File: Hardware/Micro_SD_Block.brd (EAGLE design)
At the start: 30.5 x 44.5 mm, 19 parts, among them U1 USD-SOCKETNEW, U2 EDISON_CONNECTOR_FULLMOUNTING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, U3 EDISON_CONNECTOR_FULLHEADER

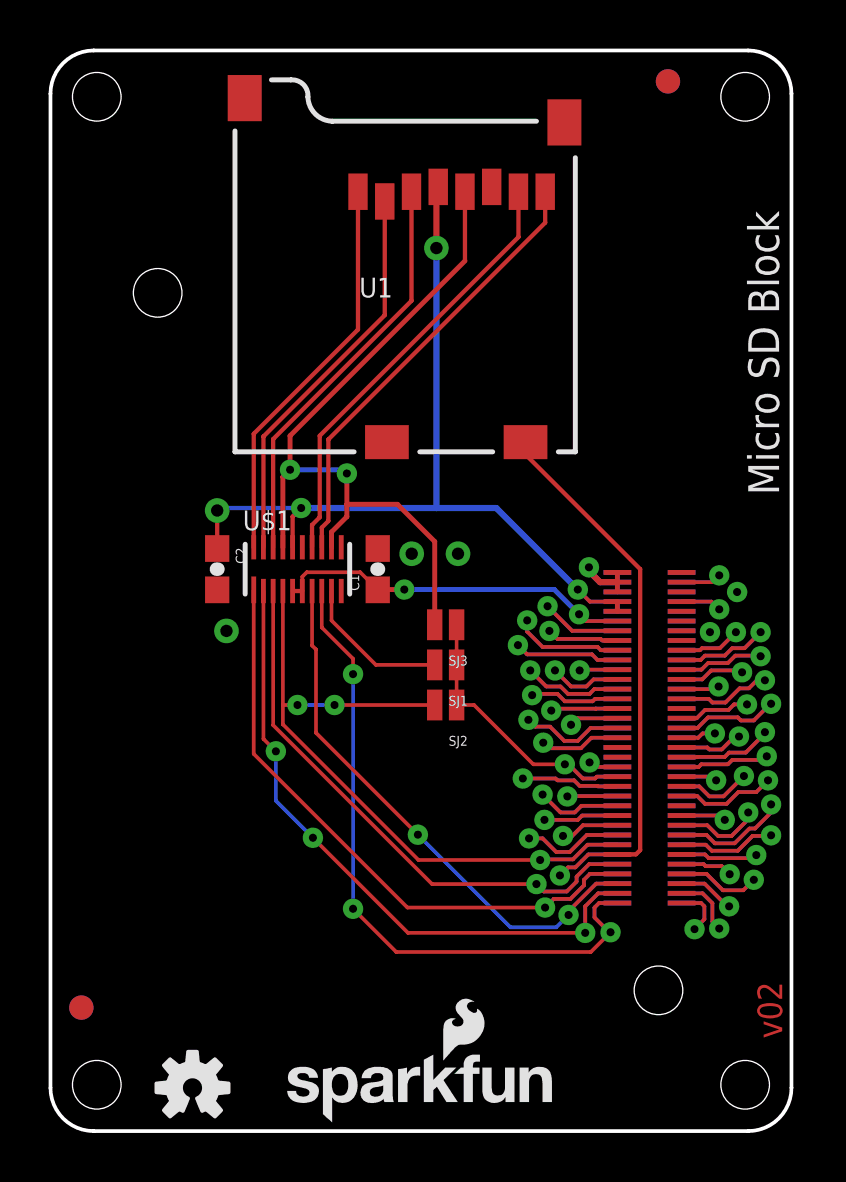
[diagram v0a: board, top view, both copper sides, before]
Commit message: removed thermals on connectors updated connector to new foot print updated version number corrected silk positions
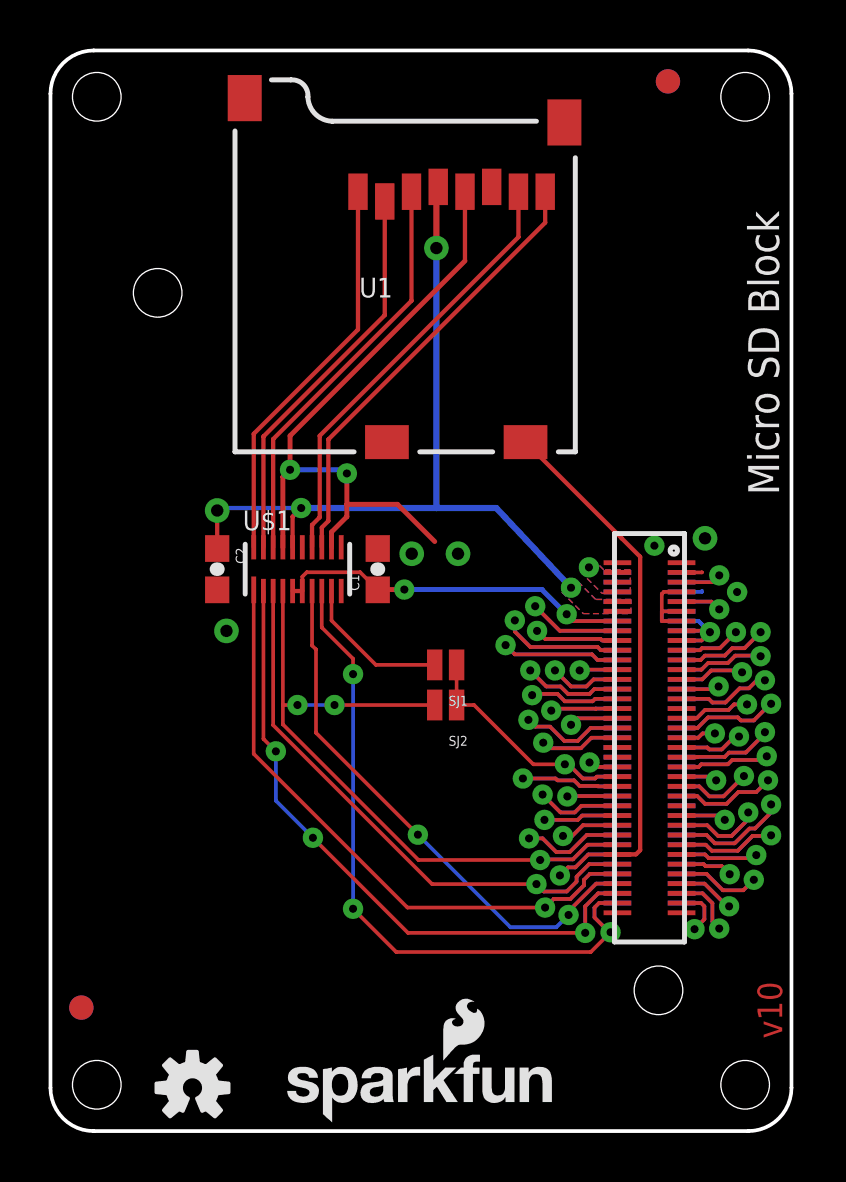
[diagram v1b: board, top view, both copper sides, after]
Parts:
- removed SJ3: JUMPER-PAD-2-NO, SparkFun-Passives:PAD-JUMPER-2-NO_NO_SILK
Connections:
- net GP84_SD_CLK_FB: no longer SJ3.1
- net SCK: no longer SJ3.2
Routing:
- net GND: track 0.00 -> 15.0 mm, vias 5 -> 7
- net 3.3V: track 37.3 -> 32.6 mm
- net VSYS: track 4.63 -> 0.00 mm
- net SCK: track 31.1 -> 27.7 mm
- net GP84_SD_CLK_FB: track 13.6 -> 12.0 mm
- net USB_VBUS: track 8.69 -> 9.71 mm
- net USB_DP: track 5.92 -> 6.94 mm
- net USB_DN: track 8.97 -> 9.99 mm
- net DCIN: track 6.58 -> 7.60 mm
- net GP77_SD_0_CD#: track 26.2 -> 26.7 mm
- net 1.8V: track 16.6 -> 17.1 mm
- added copper zone on layer 1, net 3.3V
- added copper zone on layer 16, net 3.3V
- added copper zone on layer 1, net VSYS
- added copper zone on layer 16, net VSYS
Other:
- board text added: "v10"
- board text removed: "v02"

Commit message: modified traces to eliminate bridging.  Selected FB circuit to use in production.
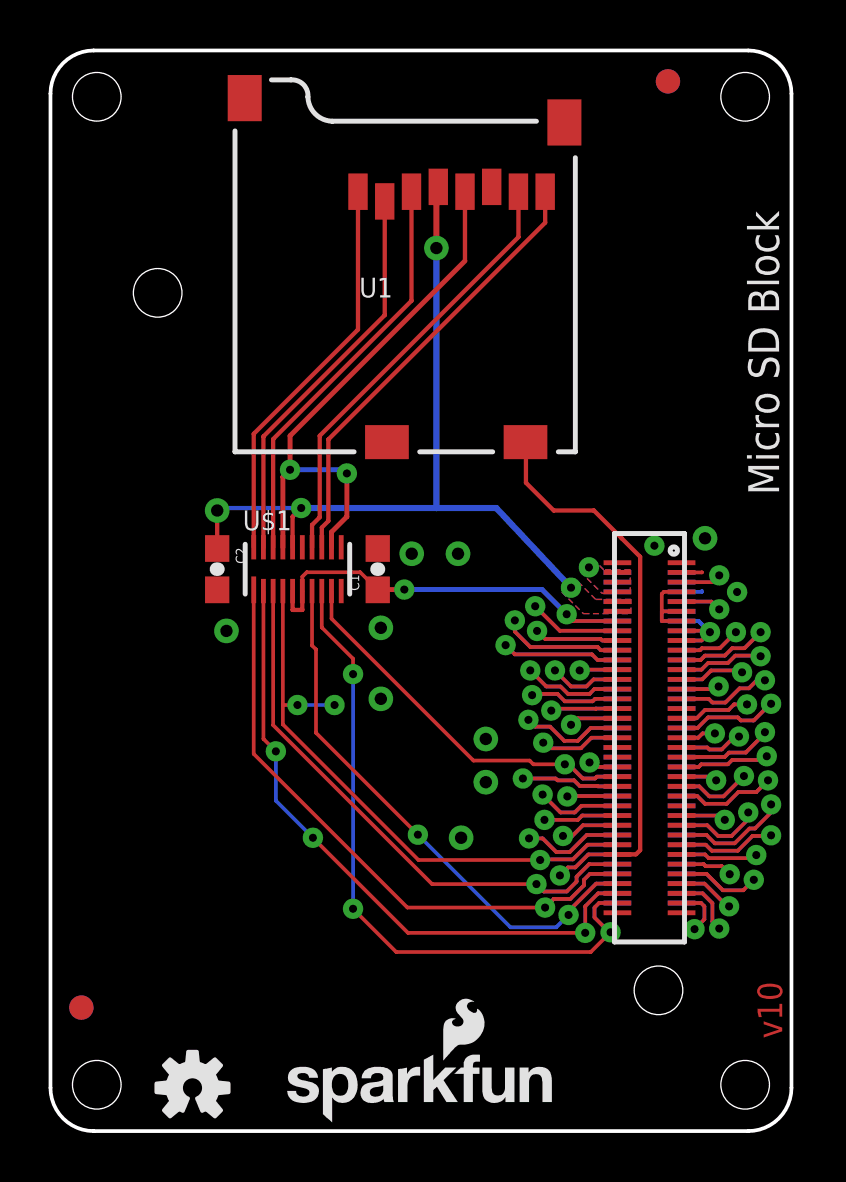
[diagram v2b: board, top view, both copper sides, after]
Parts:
- removed SJ1, SJ2: JUMPER-PAD-2-NO, SparkFun-Passives:PAD-JUMPER-2-NO_NO_SILK
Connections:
- removed net SCK_FB: SJ1.2, U$1.P$9
- net GP78_SD_0_CLK: no longer SJ2.2
- net GP84_SD_CLK_FB: now also U$1.P$9; no longer SJ1.1, SJ2.1
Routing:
- net SCK_FB: track 6.21 -> 0.00 mm
- net GP84_SD_CLK_FB: track 12.0 -> 18.1 mm
- net SCK: track 27.7 -> 23.4 mm
- net GP78_SD_0_CLK: track 31.5 -> 27.4 mm
- net 1.8V: track 17.1 -> 18.6 mm
- net GP77_SD_0_CD#: track 26.7 -> 27.7 mm
- net GND: vias 7 -> 12
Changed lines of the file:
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@@
 <attribute name="PROD_ID" value="CAP-00810" x="6.858" y="23.114" size="1.778" layer="27" rot="R270" display="off"/>
 </element>
-<element name="SJ2" library="SparkFun-Passives" package="PAD-JUMPER-2-NO_NO_SILK" value="JUMPER-PAD-2-NO" x="16.256" y="17.526" rot="R180"/>
-<element name="SJ1" library="SparkFun-Passives" package="PAD-JUMPER-2-NO_NO_SILK" value="JUMPER-PAD-2-NO" x="16.256" y="19.177" rot="R180"/>
 </elements>
 <signals>
@@
 <wire x1="25.96" y1="20.98" x2="25.146" y2="20.98" width="0.1524" layer="16"/>
 <wire x1="25.146" y1="20.98" x2="25.146" y2="21.38" width="0.1524" layer="16"/>
+<via x="13.589" y="17.78" extent="1-16" drill="0.508"/>
+<via x="17.907" y="14.351" extent="1-16" drill="0.508"/>
+<via x="16.891" y="12.065" extent="1-16" drill="0.508"/>
+<via x="17.907" y="16.129" extent="1-16" drill="0.508"/>
+<via x="13.589" y="20.701" extent="1-16" drill="0.508"/>
 </signal>
 <signal name="VSYS">
@@
 <contactref element="U2" pad="44"/>
 <contactref element="U3" pad="44"/>
-<contactref element="SJ2" pad="1"/>
-<contactref element="SJ1" pad="1"/>
-<wire x1="16.706" y1="19.177" x2="16.706" y2="17.526" width="0.1524" layer="1"/>
-<wire x1="16.706" y1="17.526" x2="17.4244" y2="17.526" width="0.1524" layer="1"/>
-<wire x1="17.4244" y1="17.526" x2="19.8628" y2="15.0876" width="0.1524" layer="1"/>
+<wire x1="19.7104" y1="15.24" x2="19.8628" y2="15.0876" width="0.1524" layer="1"/>
 <wire x1="19.8628" y1="15.0876" x2="21.1582" y2="15.0876" width="0.1524" layer="1"/>
+<contactref element="U$1" pad="P$9"/>
+<wire x1="11.56" y1="22.214" x2="11.56" y2="21.079" width="0.1524" layer="1"/>
+<wire x1="11.56" y1="21.079" x2="17.399" y2="15.24" width="0.1524" layer="1"/>
+<wire x1="17.399" y1="15.24" x2="19.7104" y2="15.24" width="0.1524" layer="1"/>
 </signal>
 <signal name="GP78_SD_0_CLK">
@@
 <contactref element="U3" pad="58"/>
 <contactref element="U$1" pad="P$4"/>
-<contactref element="SJ2" pad="2"/>
 <wire x1="9.56" y1="22.214" x2="9.56" y2="17.526" width="0.1524" layer="1"/>
 <wire x1="9.56" y1="17.526" x2="9.56" y2="16.729" width="0.1524" layer="1"/>
 <wire x1="9.56" y1="16.729" x2="15.1384" y2="11.1506" width="0.1524" layer="1"/>
 <wire x1="15.1384" y1="11.1506" x2="20.1422" y2="11.1506" width="0.1524" layer="1"/>
-<wire x1="15.806" y1="17.526" x2="11.684" y2="17.526" width="0.1524" layer="1"/>
 <via x="11.684" y="17.526" extent="1-16" drill="0.3302"/>
 <wire x1="11.684" y1="17.526" x2="10.16" y2="17.526" width="0.1524" layer="16"/>
@@
 <wire x1="24.257" y1="23.622" x2="23.495" y2="24.384" width="0.1778" layer="1"/>
 <wire x1="23.495" y1="24.384" x2="23.495" y2="24.385" width="0.1778" layer="1"/>
-<wire x1="23.495" y1="24.385" x2="19.54" y2="28.34" width="0.1778" layer="1"/>
+<wire x1="23.495" y1="24.385" x2="22.353" y2="25.527" width="0.1778" layer="1"/>
+<wire x1="22.353" y1="25.527" x2="20.701" y2="25.527" width="0.1778" layer="1"/>
+<wire x1="20.701" y1="25.527" x2="19.558" y2="26.67" width="0.1778" layer="1"/>
+<wire x1="19.558" y1="26.67" x2="19.558" y2="28.321" width="0.1778" layer="1"/>
+<wire x1="19.558" y1="28.321" x2="19.54" y2="28.34" width="0.1778" layer="1"/>
 </signal>
 <signal name="GP79_SD_0_CMD">
@@
 <contactref element="C1" pad="1"/>
 <contactref element="U$1" pad="P$6"/>
-<wire x1="9.96" y1="22.214" x2="10.36" y2="22.214" width="0.1778" layer="1"/>
 <wire x1="10.36" y1="22.214" x2="10.36" y2="22.806" width="0.1524" layer="1"/>
 <wire x1="10.36" y1="22.806" x2="10.541" y2="22.987" width="0.1524" layer="1"/>
@@
 <wire x1="14.5542" y1="22.2758" x2="20.2184" y2="22.2758" width="0.2032" layer="16"/>
 <wire x1="20.2184" y1="22.2758" x2="21.2344" y2="21.2598" width="0.2032" layer="16"/>
+<wire x1="10.36" y1="22.214" x2="10.36" y2="21.4376" width="0.1778" layer="1"/>
+<wire x1="10.36" y1="21.4376" x2="9.96" y2="21.4376" width="0.1778" layer="1"/>
+<wire x1="9.96" y1="21.4376" x2="9.96" y2="22.214" width="0.1778" layer="1"/>
 </signal>
 <signal name="FW_RCVR">
@@
 <wire x1="11.56" y1="24.641" x2="12.192" y2="25.273" width="0.2032" layer="1"/>
 <via x="12.192" y="27.051" extent="1-16" drill="0.3302"/>
-<wire x1="12.192" y1="25.273" x2="12.192" y2="25.781" width="0.2032" layer="1"/>
-<wire x1="12.192" y1="25.781" x2="12.192" y2="27.051" width="0.2032" layer="1"/>
+<wire x1="12.192" y1="25.273" x2="12.192" y2="27.051" width="0.2032" layer="1"/>
 <wire x1="12.192" y1="27.051" x2="12.0396" y2="27.2034" width="0.2032" layer="16"/>
 <wire x1="12.0396" y1="27.2034" x2="9.8552" y2="27.2034" width="0.2032" layer="16"/>
-<wire x1="15.806" y1="24.2498" x2="14.2748" y2="25.781" width="0.2032" layer="1"/>
-<wire x1="14.2748" y1="25.781" x2="12.192" y2="25.781" width="0.2032" layer="1"/>
 </signal>
 <signal name="N$5">
@@
 <wire x1="11.43" y1="28.448" x2="20.35" y2="37.368" width="0.1778" layer="1"/>
 </signal>
-<signal name="SCK_FB">
-<contactref element="U$1" pad="P$9"/>
-<contactref element="SJ1" pad="2"/>
-<wire x1="11.56" y1="22.214" x2="11.56" y2="21.0028" width="0.1524" layer="1"/>
-<wire x1="11.56" y1="21.0028" x2="13.3858" y2="19.177" width="0.1524" layer="1"/>
-<wire x1="13.3858" y1="19.177" x2="15.806" y2="19.177" width="0.1524" layer="1"/>
-</signal>
 <signal name="DCIN">
